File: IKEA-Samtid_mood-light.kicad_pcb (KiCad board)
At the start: 2 copper layers, 100 x 100 mm, 137 parts, among them IC1 ATMEGA168PA-A, P1 FTDI, P2 POWER

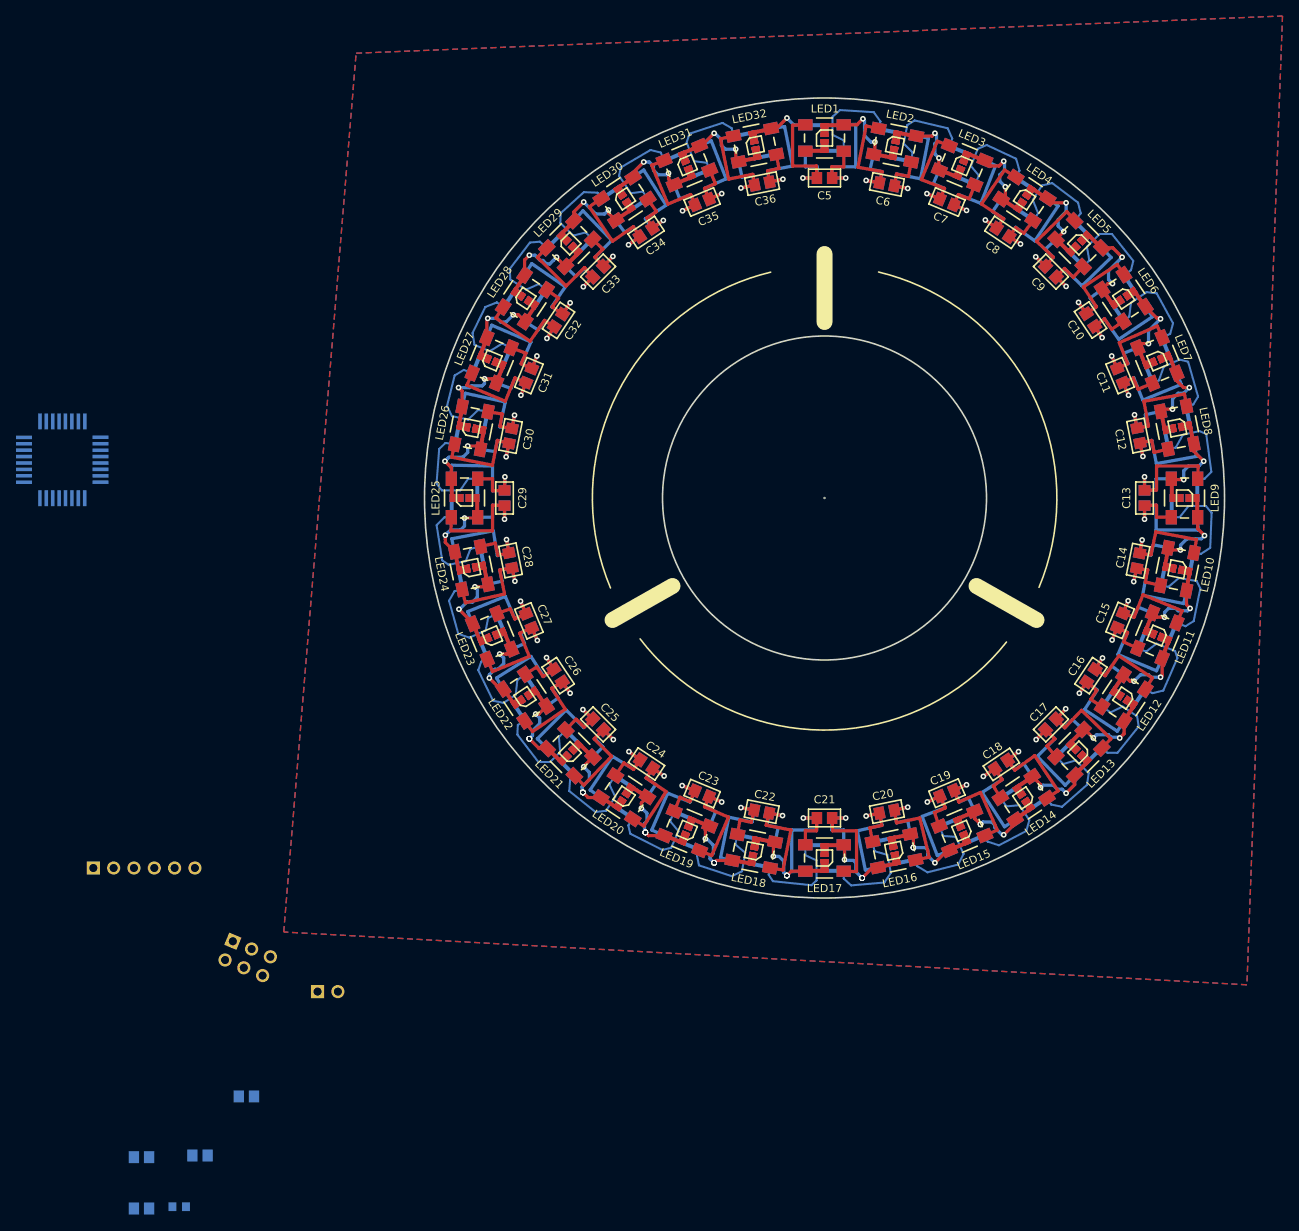
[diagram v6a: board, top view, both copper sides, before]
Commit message: Not enough free space for FTDI header :-(
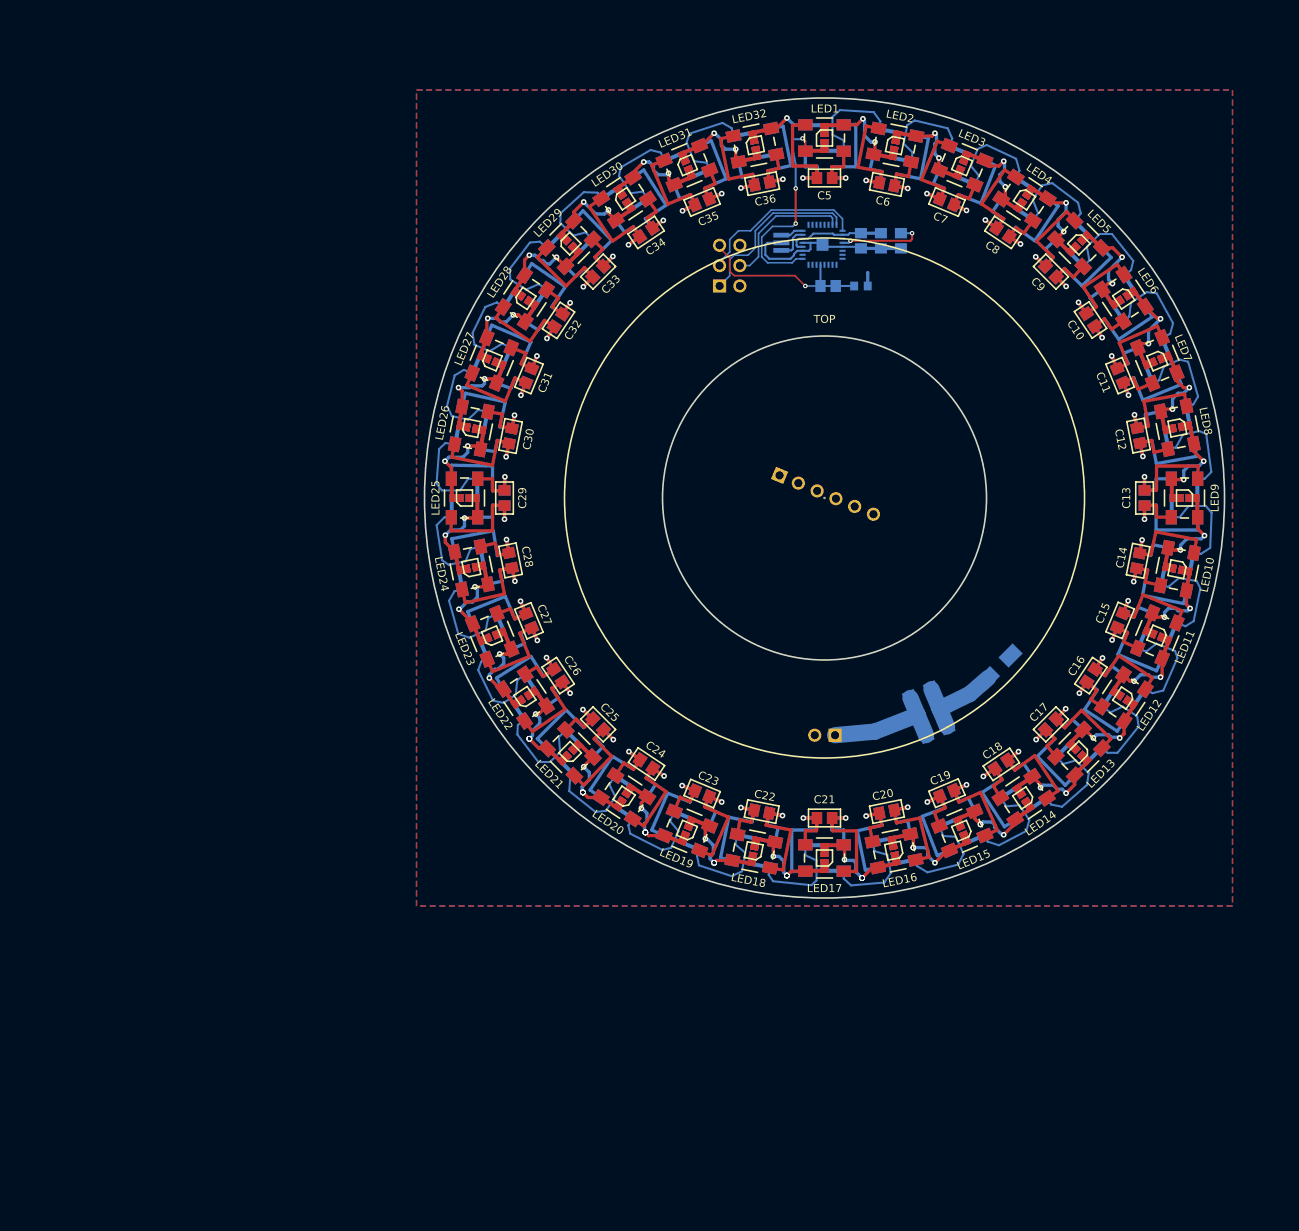
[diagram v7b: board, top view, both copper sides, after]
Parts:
- added DS1: 757-CMS04TE12, Diodes_SMD:Diode-SMA_Standard, B.Cu at (171.8, 116.1)
- added F1: 2A-poly, my_parts:MADW__R1206, B.Cu at (162.1, 119.5)
- added F2: 2A-poly, my_parts:MADW__R1206, B.Cu at (164.0, 124.1)
- added X1: CSTCE16M0V53-R0, my_parts:MADW__murata-resonator__CSTCE16M0V53-R0, B.Cu at (144.6, 63.1)
- IC1: footprint my_parts:MADW__TQFP_32_7x7 -> SMD_Packages:QFN32
- moved C3 153.8 mm to (159.6, 62.9), turned to 270 degrees
- moved C1 145.6 mm to (154.6, 62.9), turned to 270 degrees
- moved R1 143.2 mm to (154.6, 68.5)
- moved C2 142.5 mm to (157.1, 62.9), turned to 270 degrees
- moved C4 124.7 mm to (150.4, 68.5), turned to 180 degrees
- moved JP1 105.5 mm to (138.2, 66.0), turned to 270 degrees
- moved IC1 98.7 mm to (149.8, 63.4)
- moved P1 97.2 mm to (150.2, 94.6), turned to 337.5 degrees
- moved P2 69.9 mm to (150.1, 124.7), turned to 180 degrees
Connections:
- IC1 pad 10: Net-(IC1-Pad10) -> (no net)
- IC1 pad 11: Net-(IC1-Pad11) -> (no net)
- IC1 pad 12: Net-(IC1-Pad12) -> (no net)
- IC1 pad 13: Net-(IC1-Pad13) -> (no net)
- IC1 pad 14: Net-(IC1-Pad14) -> (no net)
- IC1 pad 19: Net-(IC1-Pad19) -> (no net)
- IC1 pad 2: Net-(IC1-Pad2) -> (no net)
- IC1 pad 22: Net-(IC1-Pad22) -> (no net)
- IC1 pad 23: Net-(IC1-Pad23) -> (no net)
- IC1 pad 24: Net-(IC1-Pad24) -> (no net)
- IC1 pad 25: Net-(IC1-Pad25) -> (no net)
- IC1 pad 26: Net-(IC1-Pad26) -> (no net)
- IC1 pad 27: Net-(IC1-Pad27) -> (no net)
- IC1 pad 28: Net-(IC1-Pad28) -> (no net)
- IC1 pad 32: Net-(IC1-Pad32) -> (no net)
- IC1 pad 9: Net-(IC1-Pad9) -> (no net)
- P1 pad 2: Net-(P1-Pad2) -> (no net)
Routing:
- net /WS2812B-LEDs-1/A_IN: track 0.00 -> 26.7 mm, vias 0 -> 3
- net GND: track 627.1 -> 650.3 mm
- net /DTR: track 0.00 -> 22.7 mm, vias 0 -> 1
- net /MISO: track 0.00 -> 22.0 mm
- net /SCK: track 0.00 -> 21.4 mm
- net /MOSI: track 0.00 -> 16.8 mm
- net Net-(F1-Pad1): track 0.00 -> 15.8 mm
- net +5V: track 624.9 -> 638.7 mm
- net Net-(DS1-Pad1): track 0.00 -> 12.3 mm
- net Net-(C3-Pad1): track 0.00 -> 11.0 mm, vias 0 -> 2
- net /XTAL1: track 0.00 -> 4.25 mm
- net /XTAL2: track 0.00 -> 2.88 mm
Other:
- net class power added: clearance 0.2032, trace_width 2.54, via_dia 0.7112, via_drill 0.3302
- net class signal added: clearance 0.1524, trace_width 0.2032, via_dia 0.5588, via_drill 0.254
- rule trace_min: 0.254 -> 0.2032
- rule via_min_drill: 0.3302 -> 0.254
- rule via_min_size: 0.635 -> 0.5588
- board text added: "5V"
- board text added: "BOTTOM"
- board text added: "TOP"

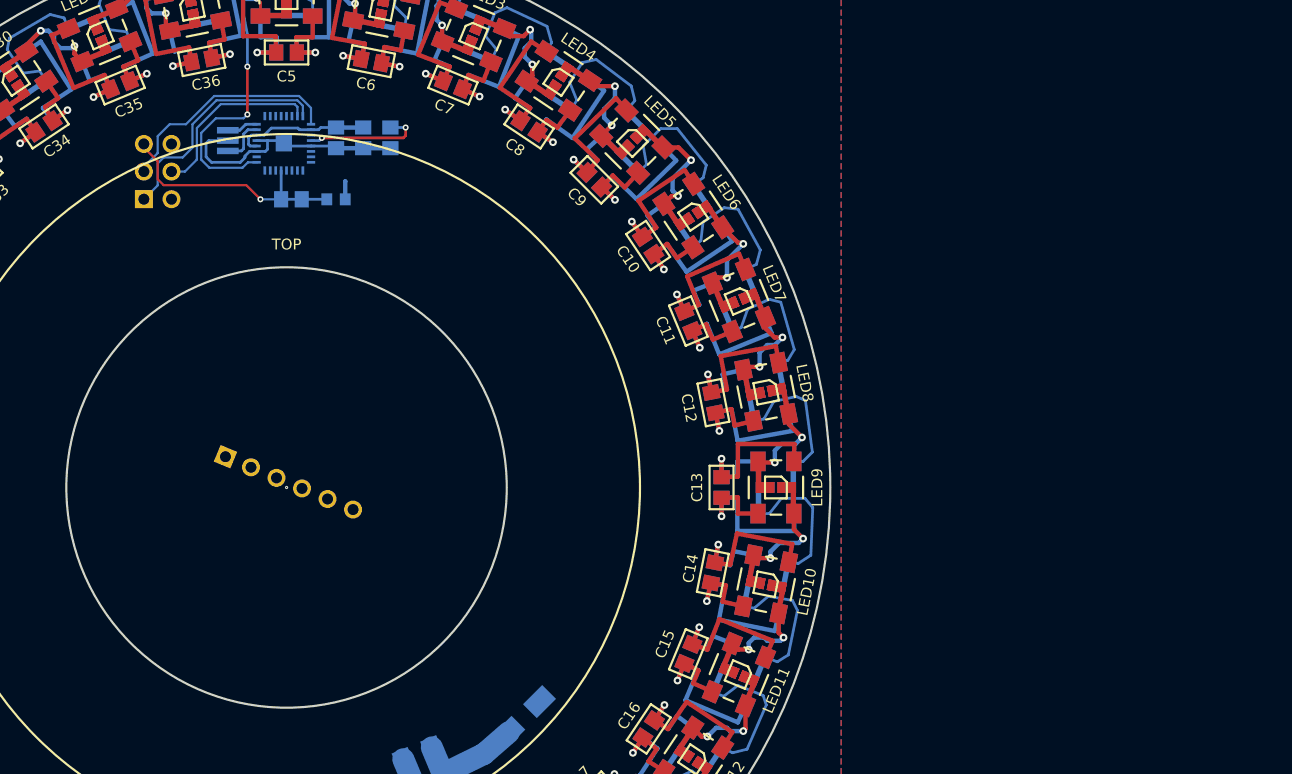
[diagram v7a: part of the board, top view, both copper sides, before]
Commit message: Had to move micro to daughter-board. Nasty routing-path creation.
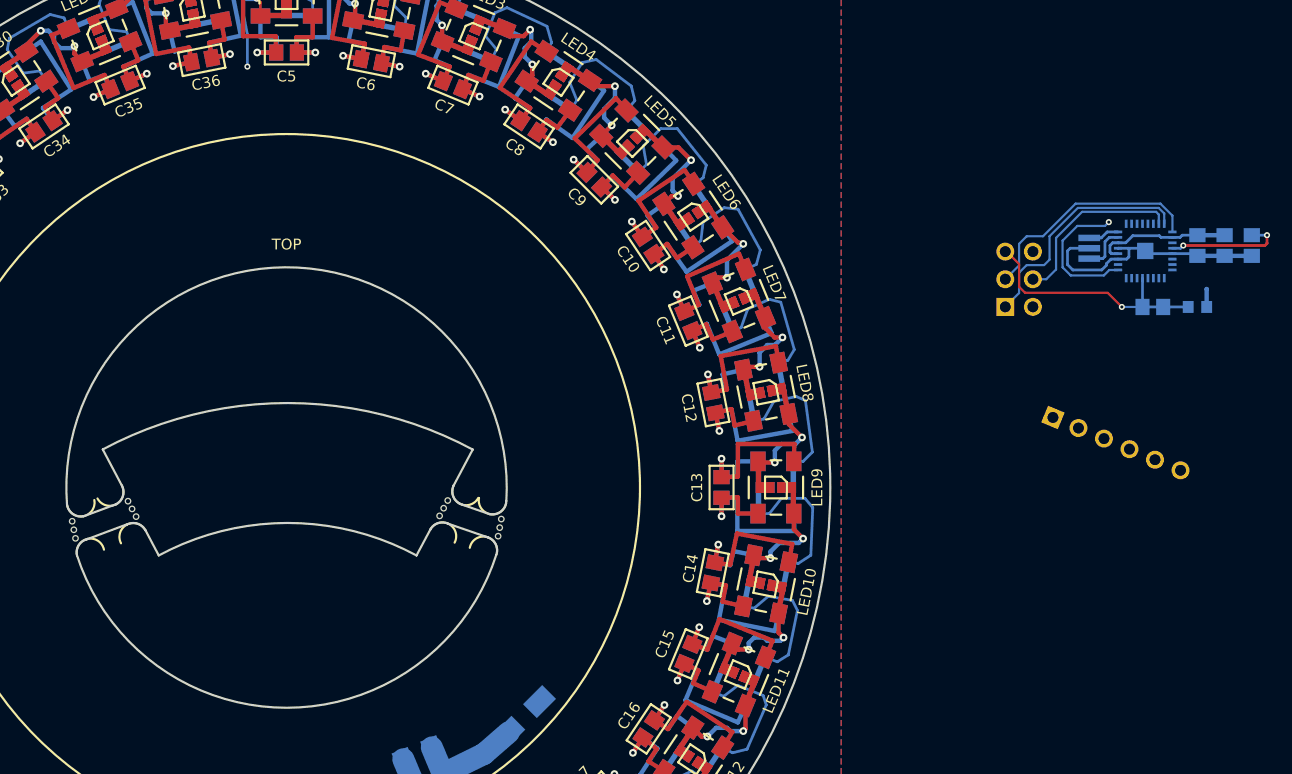
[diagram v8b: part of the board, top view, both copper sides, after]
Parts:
- added mouse-bite-2.54mm-slot: VAL**, Panelization:mouse-bite-2.54mm-slot, F.Cu at (134.8, 97.5)
- added mouse-bite-2.54mm-slot: VAL**, Panelization:mouse-bite-2.54mm-slot, F.Cu at (131.5, 98.7)
- added mouse-bite-2.54mm-slot: VAL**, Panelization:mouse-bite-2.54mm-slot, F.Cu at (168.5, 98.5)
- added mouse-bite-2.54mm-slot: VAL**, Panelization:mouse-bite-2.54mm-slot, F.Cu at (165.4, 97.4)
- moved C4 79.8 mm to (229.7, 78.4)
- moved IC1 79.8 mm to (229.0, 73.2)
- moved JP1 79.8 mm to (217.4, 75.8)
- moved X1 79.8 mm to (223.8, 73.0)
- moved C1 79.8 mm to (233.8, 72.8)
- moved C2 79.8 mm to (236.3, 72.8)
- moved C3 79.8 mm to (238.8, 72.8)
- moved R1 79.8 mm to (233.8, 78.4)
- moved P1 76.2 mm to (226.3, 91.0)
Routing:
- net /WS2812B-LEDs-1/A_IN: track 26.7 -> 22.3 mm
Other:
- outline, holes or cut-outs redrawn
